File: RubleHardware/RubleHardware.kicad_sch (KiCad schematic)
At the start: 48 parts, among them IC1 LTC3780EUH#PBF, J1_IN1 Conn_01x08_Male, J2_OUT1 Conn_01x08_Male

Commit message: feat: First stage of changes
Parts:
- C4: value 0.1uF -> 100nF; footprint (none) -> Capacitor_SMD:C_0603_1608Metric
- Cout1: footprint Capacitor_SMD:C_0402_1005Metric -> iclr:CAPC1608X90N; MFR (none) -> CL10B104KB8NNNC
- R4: footprint (none) -> Resistor_SMD:R_0402_1005Metric
- renumbered CSENS to CSENS1, Ca to Ca1, Cb to Cb1, Cf to Cf1, Css to Css1, Cvcc to Cvcc1, Da to Da1, Db to Db1, PBAD to PBAD1, RSENS+ to RSENS+1, RSENS- to RSENS-1, Rin to Rin1, Rsense to Rsense1
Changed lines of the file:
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@@
 			)
 		)
-		(property "Footprint" ""
+		(property "Footprint" "Resistor_SMD:R_0402_1005Metric"
 			(at 114.3 138.43 0)
 			(effects
@@
 			)
 		)
-		(property "Value" "0.1uF"
+		(property "Value" "100nF"
 			(at 132.588 161.798 0)
 			(effects
@@
 			)
 		)
-		(property "Footprint" ""
+		(property "Footprint" "Capacitor_SMD:C_0603_1608Metric"
 			(at 130.81 160.02 0)
 			(effects
@@
 		(on_board yes)
 		(dnp no)
-		(property "Reference" "PBAD"
+		(property "Reference" "PBAD1"
 			(at 124.206 84.328 90)
 			(effects
@@
 			(project ""
 				(path "/1d79c16d-d8ab-4199-bd03-3b802e23f067"
-					(reference "PBAD")
+					(reference "PBAD1")
 					(unit 1)
 				)
@@
 		(on_board yes)
 		(dnp no)
-		(property "Reference" "Db"
+		(property "Reference" "Db1"
 			(at 130.302 171.45 0)
 			(effects
@@
 			(project "RubleHardware"
 				(path "/1d79c16d-d8ab-4199-bd03-3b802e23f067"
-					(reference "Db")
+					(reference "Db1")
 					(unit 1)
 				)
@@
 		(dnp no)
 		(fields_autoplaced yes)
-		(property "Reference" "Rsense"
+		(property "Reference" "Rsense1"
 			(at 186.69 128.27 90)
 			(effects
@@
 			(project ""
 				(path "/1d79c16d-d8ab-4199-bd03-3b802e23f067"
-					(reference "Rsense")
+					(reference "Rsense1")
 					(unit 1)
 				)
@@
 			)
 		)
-		(property "Footprint" "Capacitor_SMD:C_0402_1005Metric"
+		(property "Footprint" "iclr:CAPC1608X90N"
 			(at 251.46 111.76 0)
 			(effects
@@
 			)
 		)
+		(property "MFR" "CL10B104KB8NNNC"
+			(at 251.46 111.76 0)
+			(effects
+				(font
+					(size 1.27 1.27)
+				)
+				(hide yes)
+			)
+		)
 		(pin "1"
 		)
@@
 		(dnp no)
 		(fields_autoplaced yes)
-		(property "Reference" "Ca"
+		(property "Reference" "Ca1"
 			(at 151.1363 92.71 90)
 			(effects
@@
 			(project ""
 				(path "/1d79c16d-d8ab-4199-bd03-3b802e23f067"
-					(reference "Ca")
+					(reference "Ca1")
 					(unit 1)
 				)
@@
 		(on_board yes)
 		(dnp no)
-		(property "Reference" "Cf"
+		(property "Reference" "Cf1"
 			(at 165.862 117.602 90)
 			(effects
@@
 			(project ""
 				(path "/1d79c16d-d8ab-4199-bd03-3b802e23f067"
-					(reference "Cf")
+					(reference "Cf1")
 					(unit 1)
 				)
@@
 		(on_board yes)
 		(dnp no)
-		(property "Reference" "RSENS-"
+		(property "Reference" "RSENS-1"
 			(at 97.79 111.76 0)
 			(effects
@@
 			(project ""
 				(path "/1d79c16d-d8ab-4199-bd03-3b802e23f067"
-					(reference "RSENS-")
+					(reference "RSENS-1")
 					(unit 1)
 				)
@@
 		(dnp no)
 		(fields_autoplaced yes)
-		(property "Reference" "Cb"
+		(property "Reference" "Cb1"
 			(at 148.5963 157.48 90)
 			(effects
@@
 			(project ""
 				(path "/1d79c16d-d8ab-4199-bd03-3b802e23f067"
-					(reference "Cb")
+					(reference "Cb1")
 					(unit 1)
 				)
@@
 		(on_board yes)
 		(dnp no)
-		(property "Reference" "Cvcc"
+		(property "Reference" "Cvcc1"
 			(at 165.1 131.318 90)
 			(effects
@@
 			(project ""
 				(path "/1d79c16d-d8ab-4199-bd03-3b802e23f067"
-					(reference "Cvcc")
+					(reference "Cvcc1")
 					(unit 1)
 				)
@@
 		(dnp no)
 		(fields_autoplaced yes)
-		(property "Reference" "Css"
+		(property "Reference" "Css1"
 			(at 104.1463 91.44 90)
 			(effects
@@
 			(project ""
 				(path "/1d79c16d-d8ab-4199-bd03-3b802e23f067"
-					(reference "Css")
+					(reference "Css1")
 					(unit 1)
 				)
@@
 		(on_board yes)
 		(dnp no)
-		(property "Reference" "Rin"
+		(property "Reference" "Rin1"
 			(at 160.528 110.49 0)
 			(effects
@@
 			(project ""
 				(path "/1d79c16d-d8ab-4199-bd03-3b802e23f067"
-					(reference "Rin")
+					(reference "Rin1")
 					(unit 1)
 				)
@@
 		(on_board yes)
 		(dnp no)
-		(property "Reference" "CSENS"
+		(property "Reference" "CSENS1"
 			(at 102.87 117.094 90)
 			(effects
@@
 			(project ""
 				(path "/1d79c16d-d8ab-4199-bd03-3b802e23f067"
-					(reference "CSENS")
+					(reference "CSENS1")
 					(unit 1)
 				)
@@
 		(on_board yes)
 		(dnp no)
-		(property "Reference" "RSENS+"
+		(property "Reference" "RSENS+1"
 			(at 113.284 111.76 0)
 			(effects
@@
 			(project ""
 				(path "/1d79c16d-d8ab-4199-bd03-3b802e23f067"
-					(reference "RSENS+")
+					(reference "RSENS+1")
 					(unit 1)
 				)
@@
 		(on_board yes)
 		(dnp no)
-		(property "Reference" "Da"
+		(property "Reference" "Da1"
 			(at 151.384 85.344 0)
 			(effects
@@
 			(project "RubleHardware"
 				(path "/1d79c16d-d8ab-4199-bd03-3b802e23f067"
-					(reference "Da")
+					(reference "Da1")
 					(unit 1)
 				)

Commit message: trying something out
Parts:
- Cin2, Cin3, Cin4: footprint iclr:CAPC6050X550N -> iclr:CAPC2012X145N; MFR CKG57NX5R1H226M500JH -> C2012X5R1V226M125AC
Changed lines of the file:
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@@
 			)
 		)
-		(property "Footprint" "iclr:CAPC6050X550N"
+		(property "Footprint" "iclr:CAPC2012X145N"
 			(at 274.32 132.08 0)
 			(effects
@@
 			)
 		)
-		(property "MFR" "CKG57NX5R1H226M500JH"
+		(property "MFR" "C2012X5R1V226M125AC"
 			(at 274.32 132.08 0)
 			(effects
@@
 			)
 		)
-		(property "Footprint" "iclr:CAPC6050X550N"
+		(property "Footprint" "iclr:CAPC2012X145N"
 			(at 251.46 132.08 0)
 			(effects
@@
 			)
 		)
-		(property "MFR" "CKG57NX5R1H226M500JH"
+		(property "MFR" "C2012X5R1V226M125AC"
 			(at 251.46 132.08 0)
 			(effects
@@
 			)
 		)
-		(property "Footprint" "iclr:CAPC6050X550N"
+		(property "Footprint" "iclr:CAPC2012X145N"
 			(at 264.16 132.08 0)
 			(effects
@@
 			)
 		)
-		(property "MFR" "CKG57NX5R1H226M500JH"
+		(property "MFR" "C2012X5R1V226M125AC"
 			(at 264.16 132.08 0)
 			(effects

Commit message: feat: v0.4 ready
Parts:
- added R5: 15k, Resistor_SMD:R_0402_1005Metric, symbol Device:R_Small
- Rsense1: value 1.9m -> 5m; footprint Resistor_SMD:R_0402_1005Metric_Pad0.72x0.64mm_HandSolder -> iclr:RESC6432X67N
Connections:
- net INTVCC: now also R5.1
- net at IC1.8 (PLLFTR), R4.2: now also R5.2
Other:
- note added: "Voltage divider to get PLLFTR held at ~2.4V"
- moved on the sheet: R4
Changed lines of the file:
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@@
 		)
 	)
+	(text "Voltage divider to get \nPLLFTR held at ~2.4V\n"
+		(exclude_from_sim no)
+		(at 103.378 151.384 0)
+		(effects
+			(font
+				(size 1.27 1.27)
+			)
+		)
+	)
 	(text "24V"
 		(exclude_from_sim no)
@@
 	)
 	(junction
+		(at 116.84 138.43)
+		(diameter 0)
+		(color 0 0 0 0)
+	)
+	(junction
 		(at 261.62 35.56)
 		(diameter 0)
@@
 	)
 	(junction
+		(at 107.95 138.43)
+		(diameter 0)
+		(color 0 0 0 0)
+	)
+	(junction
 		(at 205.74 123.19)
 		(diameter 0)
@@
 	)
 	(junction
-		(at 110.49 138.43)
-		(diameter 0)
-		(color 0 0 0 0)
-	)
-	(junction
 		(at 264.16 127)
 		(diameter 0)
@@
 	(wire
 		(pts
-			(xy 251.46 127) (xy 257.81 127)
+			(xy 115.57 138.43) (xy 116.84 138.43)
 		)
 		(stroke
@@
 	(wire
 		(pts
-			(xy 240.03 137.16) (xy 251.46 137.16)
+			(xy 251.46 127) (xy 257.81 127)
 		)
 		(stroke
@@
 	(wire
 		(pts
-			(xy 257.81 142.24) (xy 261.62 142.24)
+			(xy 240.03 137.16) (xy 251.46 137.16)
 		)
 		(stroke
@@
 	(wire
 		(pts
-			(xy 218.44 121.92) (xy 218.44 123.19)
+			(xy 257.81 142.24) (xy 261.62 142.24)
 		)
 		(stroke
@@
 	(wire
 		(pts
-			(xy 110.49 138.43) (xy 111.76 138.43)
+			(xy 218.44 121.92) (xy 218.44 123.19)
 		)
 		(stroke
@@
 	(wire
 		(pts
+			(xy 116.84 139.7) (xy 116.84 138.43)
+		)
+		(stroke
+			(width 0)
+			(type default)
+		)
+	)
+	(wire
+		(pts
 			(xy 116.84 162.56) (xy 116.84 165.1)
 		)
@@
 	(wire
 		(pts
+			(xy 107.95 138.43) (xy 107.95 142.24)
+		)
+		(stroke
+			(width 0)
+			(type default)
+		)
+	)
+	(wire
+		(pts
 			(xy 190.5 133.35) (xy 198.12 133.35)
 		)
@@
 	(wire
 		(pts
+			(xy 116.84 138.43) (xy 118.11 138.43)
+		)
+		(stroke
+			(width 0)
+			(type default)
+		)
+	)
+	(wire
+		(pts
 			(xy 198.12 133.35) (xy 198.12 139.7)
 		)
@@
 	(wire
 		(pts
+			(xy 107.95 138.43) (xy 110.49 138.43)
+		)
+		(stroke
+			(width 0)
+			(type default)
+		)
+	)
+	(wire
+		(pts
 			(xy 106.68 109.22) (xy 106.68 110.49)
 		)
@@
 	(wire
 		(pts
-			(xy 116.84 138.43) (xy 118.11 138.43)
-		)
-		(stroke
-			(width 0)
-			(type default)
-		)
-	)
-	(wire
-		(pts
 			(xy 146.05 76.2) (xy 146.05 82.55)
 		)
@@
 	(wire
 		(pts
-			(xy 110.49 135.89) (xy 110.49 138.43)
+			(xy 107.95 135.89) (xy 107.95 138.43)
 		)
 		(stroke
@@
 	(wire
 		(pts
-			(xy 110.49 138.43) (xy 110.49 142.24)
-		)
-		(stroke
-			(width 0)
-			(type default)
-		)
-	)
-	(wire
-		(pts
 			(xy 92.71 35.56) (xy 97.79 35.56)
 		)
@@
 	(wire
 		(pts
+			(xy 116.84 144.78) (xy 116.84 147.32)
+		)
+		(stroke
+			(width 0)
+			(type default)
+		)
+	)
+	(wire
+		(pts
 			(xy 100.33 35.56) (xy 102.87 35.56)
 		)
@@
 	(wire
 		(pts
-			(xy 118.11 135.89) (xy 110.49 135.89)
+			(xy 118.11 135.89) (xy 107.95 135.89)
 		)
 		(stroke
@@
 		)
 	)
+	(label "INTVCC"
+		(at 116.84 147.32 270)
+		(effects
+			(font
+				(size 1.27 1.27)
+			)
+			(justify right bottom)
+		)
+	)
 	(label "ICVIN"
 		(at 242.57 144.78 270)
@@
 	)
 	(label "GNDS"
-		(at 110.49 142.24 270)
+		(at 107.95 142.24 270)
 		(effects
 			(font
@@
 	(symbol
 		(lib_id "Device:R_Small")
-		(at 114.3 138.43 90)
+		(at 113.03 138.43 90)
 		(unit 1)
 		(exclude_from_sim no)
@@
 		(dnp no)
 		(property "Reference" "R4"
-			(at 114.046 140.97 90)
+			(at 112.776 140.97 90)
 			(effects
 				(font
@@
 		)
 		(property "Value" "10k"
-			(at 114.3 143.256 90)
+			(at 113.03 143.256 90)
 			(effects
 				(font
@@
 		)
 		(property "Footprint" "Resistor_SMD:R_0402_1005Metric"
-			(at 114.3 138.43 0)
+			(at 113.03 138.43 0)
 			(effects
 				(font
@@
 		)
 		(property "Datasheet" "~"
-			(at 114.3 138.43 0)
+			(at 113.03 138.43 0)
 			(effects
 				(font
@@
 		)
 		(property "Description" "Resistor, small symbol"
-			(at 114.3 138.43 0)
+			(at 113.03 138.43 0)
 			(effects
 				(font
@@
 			)
 		)
-		(property "Value" "1.9m"
+		(property "Value" "5m"
 			(at 186.69 130.81 90)
 			(effects
@@
 			)
 		)
-		(property "Footprint" "Resistor_SMD:R_0402_1005Metric_Pad0.72x0.64mm_HandSolder"
+		(property "Footprint" "iclr:RESC6432X67N"
 			(at 186.69 133.35 0)
 			(effects
@@
 			)
 		)
-		(property "Description" "Resistor, small symbol"
+		(property "Description" "PMR100HZPFU5L00"
 			(at 186.69 133.35 0)
 			(effects
@@
 					(unit 1)
 				)
+			)
+		)
+	)
+	(symbol
+		(lib_id "Device:R_Small")
+		(at 116.84 142.24 180)
+		(unit 1)
+		(exclude_from_sim no)
+		(in_bom yes)
+		(on_board yes)
+		(dnp no)
+		(property "Reference" "R5"
+			(at 119.38 142.494 90)
+			(effects
+				(font
+					(size 1.27 1.27)
+				)
+			)
+		)
+		(property "Value" "15k"
+			(at 121.666 142.24 90)
+			(effects
+				(font
+					(size 1.27 1.27)
+				)
+			)
+		)
+		(property "Footprint" "Resistor_SMD:R_0402_1005Metric"
+			(at 116.84 142.24 0)
+			(effects
+				(font
+					(size 1.27 1.27)
+				)
+				(hide yes)
+			)
+		)
+		(property "Datasheet" "~"
+			(at 116.84 142.24 0)
+			(effects
+				(font
+					(size 1.27 1.27)
+				)
+				(hide yes)
+			)
+		)
+		(property "Description" "Resistor, small symbol"
+			(at 116.84 142.24 0)
+			(effects
+				(font
+					(size 1.27 1.27)
+				)
+				(hide yes)
+			)
+		)
+		(pin "2"
+		)
+		(pin "1"
+		)
+		(instances
+			(project "RubleHardware"
+				(path "/1d79c16d-d8ab-4199-bd03-3b802e23f067"
+					(reference "R5")
+					(unit 1)
+				)

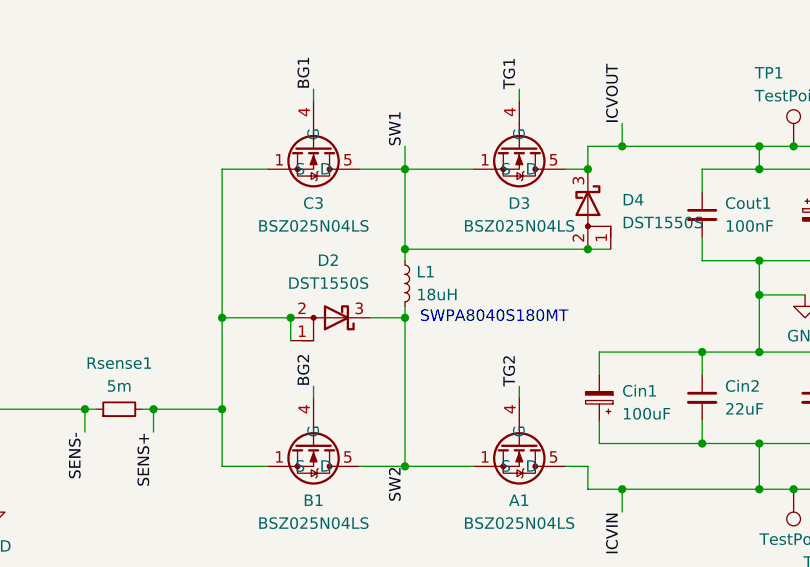
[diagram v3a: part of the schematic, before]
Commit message: Minor tweaks
Moved GND mounting holes away from edge
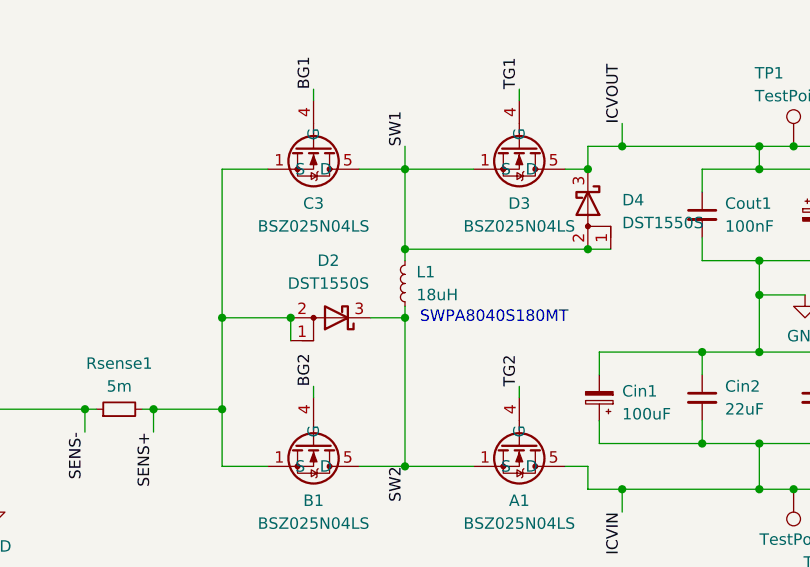
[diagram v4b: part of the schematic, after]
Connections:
- net SW1: now also L1.2; no longer L1.1
- net SW2: now also L1.1; no longer L1.2
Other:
- moved on the sheet: L1
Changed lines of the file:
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@@
 	(symbol
 		(lib_id "Device:L_Small")
-		(at 218.44 119.38 0)
+		(at 218.44 119.38 180)
 		(unit 1)
 		(exclude_from_sim no)
@@
 					(size 1.27 1.27)
 				)
-				(justify left)
+				(justify right)
 			)
 		)
@@
 					(size 1.27 1.27)
 				)
-				(justify left)
+				(justify right)
 			)
 		)
